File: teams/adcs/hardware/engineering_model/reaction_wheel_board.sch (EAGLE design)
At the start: 78 parts

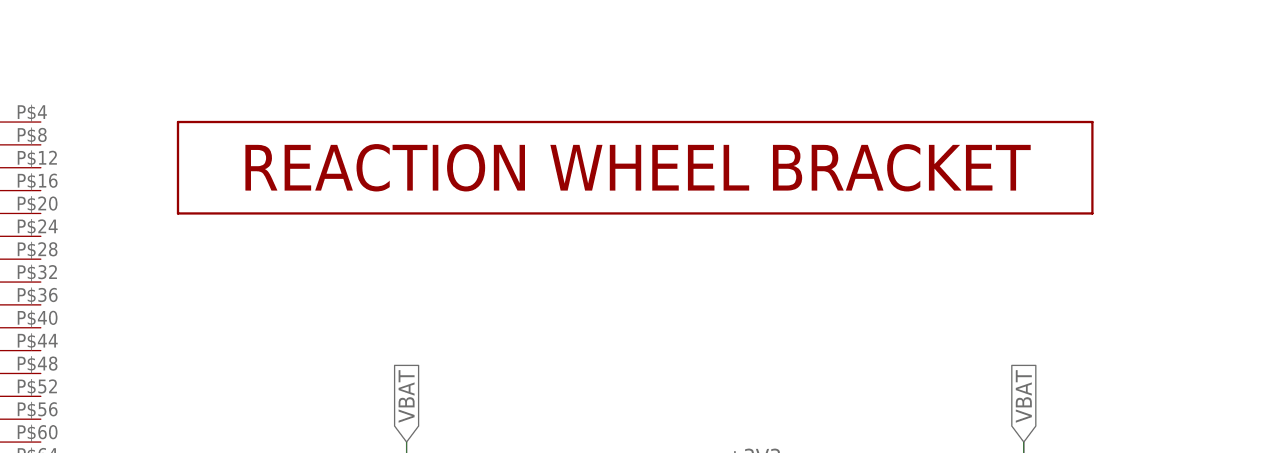
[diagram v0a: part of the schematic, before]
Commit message: ADCS/RW: Make some room for the new motor bracket
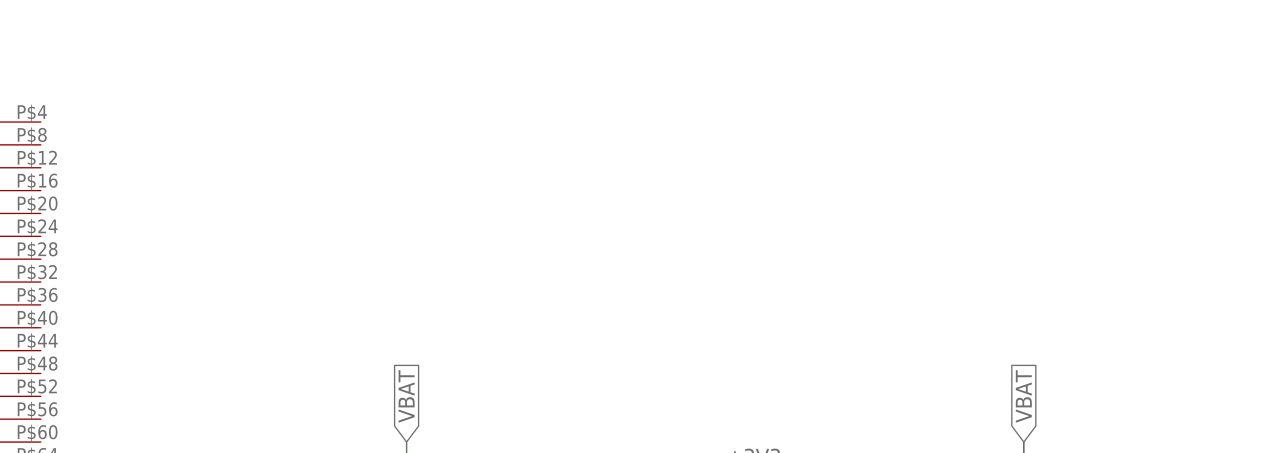
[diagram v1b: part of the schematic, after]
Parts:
- removed U$9: REACTION_WHEEL_BRACKET, DubSat1 Components:REACTION_WHEEL_BRACKET
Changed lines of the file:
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@@
 <part name="+3V1" library="supply1" library_urn="urn:adsk.eagle:library:371" deviceset="+3V3" device=""/>
 <part name="P+1" library="supply1" library_urn="urn:adsk.eagle:library:371" deviceset="+5V" device=""/>
-<part name="U$9" library="DubSat1 Components" deviceset="REACTION_WHEEL_BRACKET" device=""/>
 <part name="U$7" library="DubSat1 Components" deviceset="DRV10970" device=""/>
 <part name="C1" library="rcl" library_urn="urn:adsk.eagle:library:334" deviceset="C-US" device="C1206" package3d_urn="urn:adsk.eagle:package:23618/2" value="2.2uF"/>
@@
 <instance part="+3V1" gate="G$1" x="-63.5" y="-55.88" rot="R90"/>
 <instance part="P+1" gate="1" x="-63.5" y="-35.56" rot="R90"/>
-<instance part="U$9" gate="G$1" x="157.48" y="71.12"/>
 <instance part="U$7" gate="G$1" x="-2.54" y="-246.38" rot="R270"/>
 <instance part="C1" gate="G$1" x="15.24" y="-274.32"/>

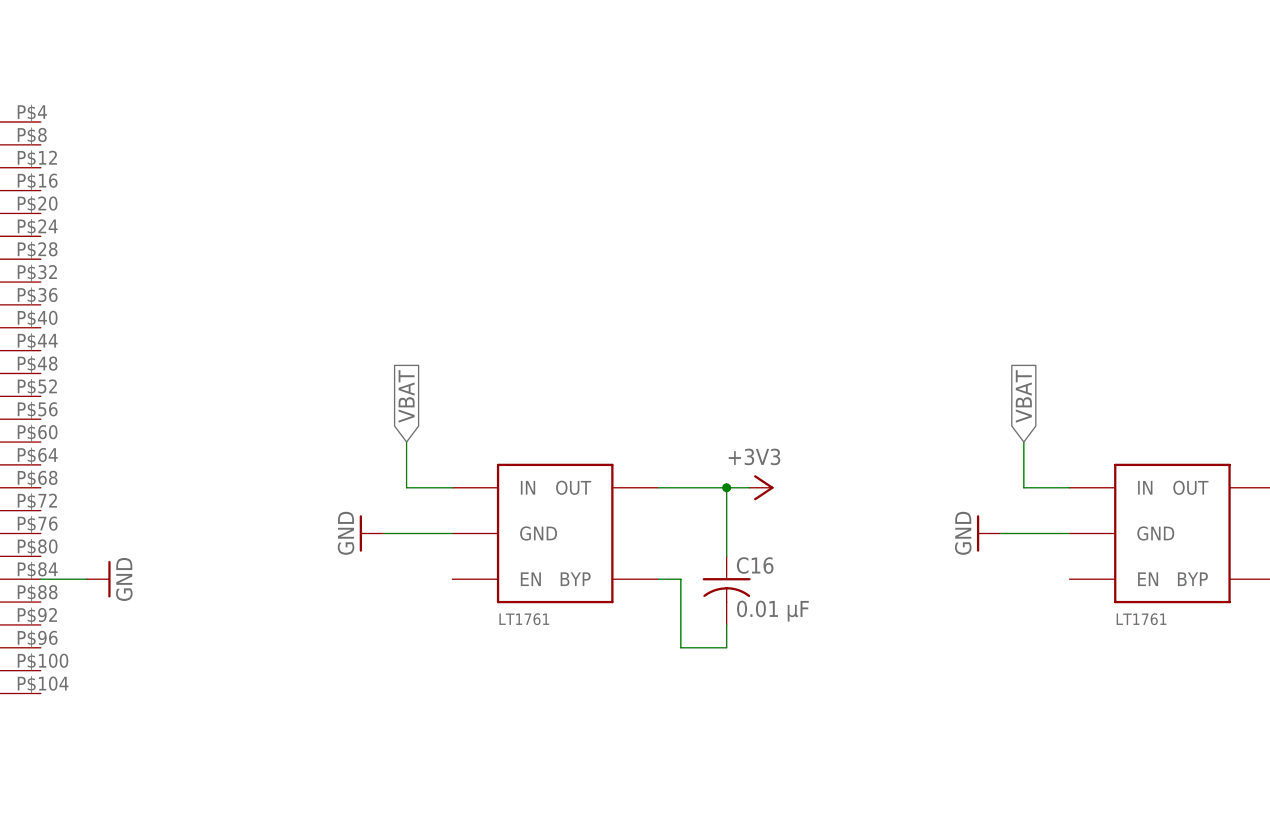
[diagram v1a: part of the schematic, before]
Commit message: ADCS/RW: Tie ENABLE pins high on LDOs
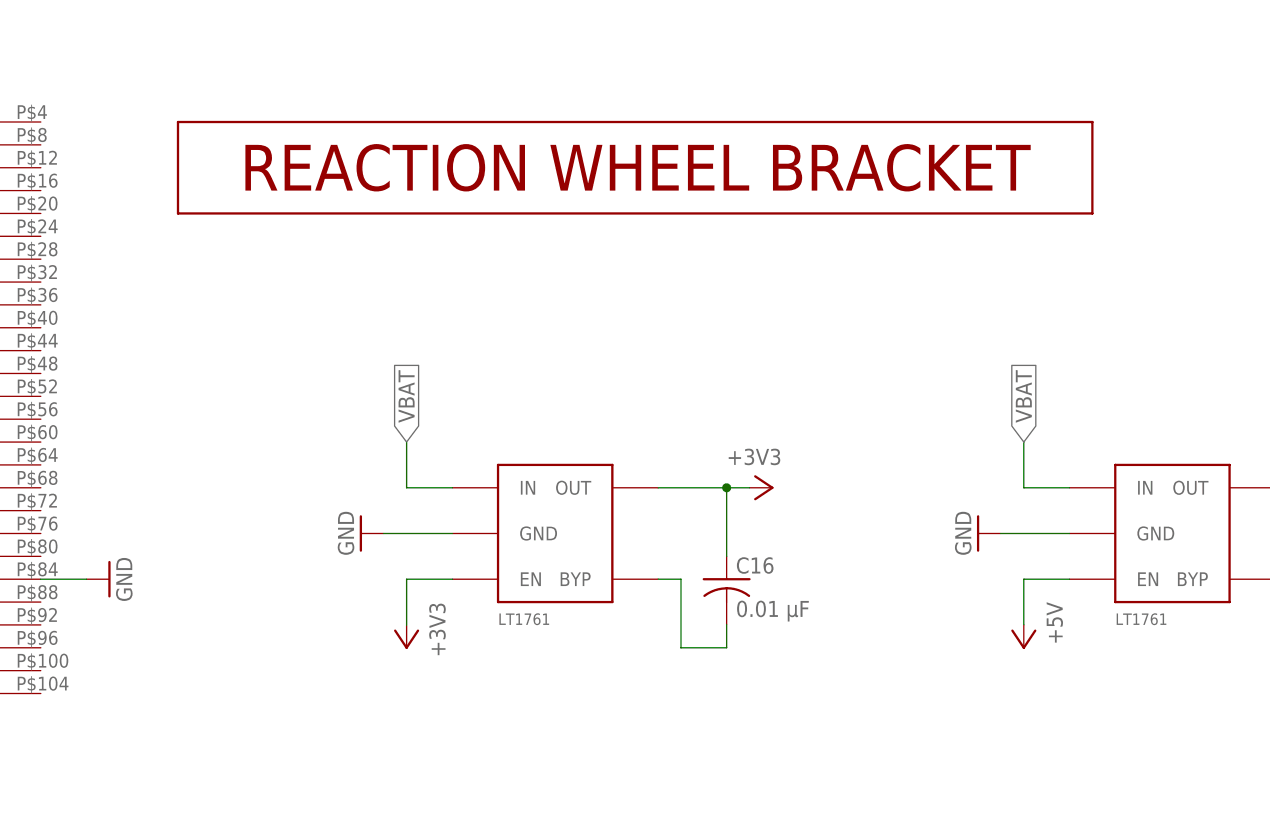
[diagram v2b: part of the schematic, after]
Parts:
- added U$9: REACTION_WHEEL_BRACKET, DubSat1 Components:REACTION_WHEEL_BRACKET
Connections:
- net +3V3: now also LDO_3V3.EN
- net +5V: now also LDO_5V.EN
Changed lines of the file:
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@@
 <part name="+3V1" library="supply1" library_urn="urn:adsk.eagle:library:371" deviceset="+3V3" device=""/>
 <part name="P+1" library="supply1" library_urn="urn:adsk.eagle:library:371" deviceset="+5V" device=""/>
+<part name="U$9" library="DubSat1 Components" deviceset="REACTION_WHEEL_BRACKET" device=""/>
 <part name="U$7" library="DubSat1 Components" deviceset="DRV10970" device=""/>
 <part name="C1" library="rcl" library_urn="urn:adsk.eagle:library:334" deviceset="C-US" device="C1206" package3d_urn="urn:adsk.eagle:package:23618/2" value="2.2uF"/>
@@
 <part name="R14" library="rcl" library_urn="urn:adsk.eagle:library:334" deviceset="R-US_" device="R0805" package3d_urn="urn:adsk.eagle:package:23553/2"/>
 <part name="GND49" library="supply1" library_urn="urn:adsk.eagle:library:371" deviceset="GND" device=""/>
+<part name="+3V2" library="supply1" library_urn="urn:adsk.eagle:library:371" deviceset="+3V3" device=""/>
+<part name="P+2" library="supply1" library_urn="urn:adsk.eagle:library:371" deviceset="+5V" device=""/>
 </parts>
 <sheets>
@@
 <instance part="+3V1" gate="G$1" x="-63.5" y="-55.88" rot="R90"/>
 <instance part="P+1" gate="1" x="-63.5" y="-35.56" rot="R90"/>
+<instance part="U$9" gate="G$1" x="157.48" y="71.12"/>
 <instance part="U$7" gate="G$1" x="-2.54" y="-246.38" rot="R270"/>
 <instance part="C1" gate="G$1" x="15.24" y="-274.32"/>
@@
 <instance part="R14" gate="G$1" x="294.64" y="45.72" rot="R90"/>
 <instance part="GND49" gate="1" x="294.64" y="38.1" rot="MR0"/>
+<instance part="+3V2" gate="G$1" x="129.54" y="17.78" rot="R180"/>
+<instance part="P+2" gate="1" x="198.12" y="17.78" rot="R180"/>
 </instances>
 <busses>
@@
 <junction x="251.46" y="-38.1"/>
 </segment>
+<segment>
+<pinref part="+3V2" gate="G$1" pin="+3V3"/>
+<pinref part="LDO_3V3" gate="G$1" pin="EN"/>
+<wire x1="129.54" y1="20.32" x2="129.54" y2="25.4" width="0.1524" layer="91"/>
+<wire x1="129.54" y1="25.4" x2="134.62" y2="25.4" width="0.1524" layer="91"/>
+</segment>
 </net>
 <net name="+5V" class="0">
@@
 <wire x1="256.54" y1="-30.48" x2="236.22" y2="-30.48" width="0.1524" layer="91"/>
 </segment>
-</net>
+<segment>
+<pinref part="P+2" gate="1" pin="+5V"/>
+<pinref part="LDO_5V" gate="G$1" pin="EN"/>
+<wire x1="198.12" y1="20.32" x2="198.12" y2="25.4" width="0.1524" layer="91"/>
+<wire x1="198.12" y1="25.4" x2="203.2" y2="25.4" width="0.1524" layer="91"/>
+</segment>
+</net>

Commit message: ADCS/RW: Tie LDO ENABLE input high
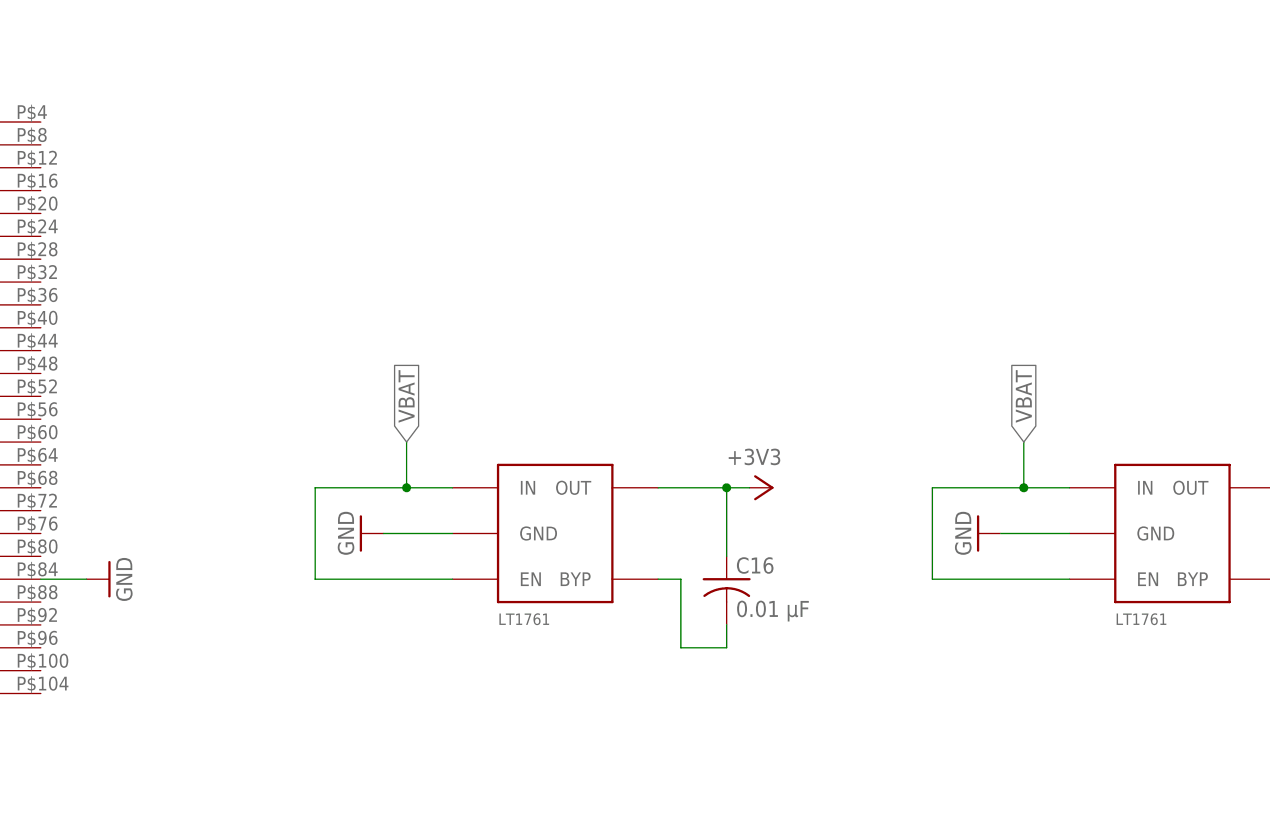
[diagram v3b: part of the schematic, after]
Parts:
- removed U$9: REACTION_WHEEL_BRACKET, DubSat1 Components:REACTION_WHEEL_BRACKET
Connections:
- net +3V3: no longer LDO_3V3.EN
- net +5V: no longer LDO_5V.EN
- net VBAT: now also LDO_3V3.EN, LDO_5V.EN
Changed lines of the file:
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@@
 <part name="+3V1" library="supply1" library_urn="urn:adsk.eagle:library:371" deviceset="+3V3" device=""/>
 <part name="P+1" library="supply1" library_urn="urn:adsk.eagle:library:371" deviceset="+5V" device=""/>
-<part name="U$9" library="DubSat1 Components" deviceset="REACTION_WHEEL_BRACKET" device=""/>
 <part name="U$7" library="DubSat1 Components" deviceset="DRV10970" device=""/>
 <part name="C1" library="rcl" library_urn="urn:adsk.eagle:library:334" deviceset="C-US" device="C1206" package3d_urn="urn:adsk.eagle:package:23618/2" value="2.2uF"/>
@@
 <part name="R14" library="rcl" library_urn="urn:adsk.eagle:library:334" deviceset="R-US_" device="R0805" package3d_urn="urn:adsk.eagle:package:23553/2"/>
 <part name="GND49" library="supply1" library_urn="urn:adsk.eagle:library:371" deviceset="GND" device=""/>
-<part name="+3V2" library="supply1" library_urn="urn:adsk.eagle:library:371" deviceset="+3V3" device=""/>
-<part name="P+2" library="supply1" library_urn="urn:adsk.eagle:library:371" deviceset="+5V" device=""/>
 </parts>
 <sheets>
@@
 <instance part="+3V1" gate="G$1" x="-63.5" y="-55.88" rot="R90"/>
 <instance part="P+1" gate="1" x="-63.5" y="-35.56" rot="R90"/>
-<instance part="U$9" gate="G$1" x="157.48" y="71.12"/>
 <instance part="U$7" gate="G$1" x="-2.54" y="-246.38" rot="R270"/>
 <instance part="C1" gate="G$1" x="15.24" y="-274.32"/>
@@
 <instance part="R14" gate="G$1" x="294.64" y="45.72" rot="R90"/>
 <instance part="GND49" gate="1" x="294.64" y="38.1" rot="MR0"/>
-<instance part="+3V2" gate="G$1" x="129.54" y="17.78" rot="R180"/>
-<instance part="P+2" gate="1" x="198.12" y="17.78" rot="R180"/>
 </instances>
 <busses>
@@
 <wire x1="129.54" y1="35.56" x2="129.54" y2="40.64" width="0.1524" layer="91"/>
 <label x="129.54" y="40.64" size="1.778" layer="95" rot="R90" xref="yes"/>
+<wire x1="129.54" y1="35.56" x2="119.38" y2="35.56" width="0.1524" layer="91"/>
+<junction x="129.54" y="35.56"/>
+<pinref part="LDO_3V3" gate="G$1" pin="EN"/>
+<wire x1="119.38" y1="35.56" x2="119.38" y2="25.4" width="0.1524" layer="91"/>
+<wire x1="119.38" y1="25.4" x2="134.62" y2="25.4" width="0.1524" layer="91"/>
 </segment>
 <segment>
@@
 <wire x1="198.12" y1="35.56" x2="198.12" y2="40.64" width="0.1524" layer="91"/>
 <label x="198.12" y="40.64" size="1.778" layer="95" rot="R90" xref="yes"/>
+<wire x1="198.12" y1="35.56" x2="187.96" y2="35.56" width="0.1524" layer="91"/>
+<junction x="198.12" y="35.56"/>
+<pinref part="LDO_5V" gate="G$1" pin="EN"/>
+<wire x1="187.96" y1="35.56" x2="187.96" y2="25.4" width="0.1524" layer="91"/>
+<wire x1="187.96" y1="25.4" x2="203.2" y2="25.4" width="0.1524" layer="91"/>
 </segment>
 <segment>
@@
 <junction x="251.46" y="-38.1"/>
 </segment>
-<segment>
-<pinref part="+3V2" gate="G$1" pin="+3V3"/>
-<pinref part="LDO_3V3" gate="G$1" pin="EN"/>
-<wire x1="129.54" y1="20.32" x2="129.54" y2="25.4" width="0.1524" layer="91"/>
-<wire x1="129.54" y1="25.4" x2="134.62" y2="25.4" width="0.1524" layer="91"/>
-</segment>
 </net>
 <net name="+5V" class="0">
@@
 <wire x1="256.54" y1="-30.48" x2="236.22" y2="-30.48" width="0.1524" layer="91"/>
 </segment>
-<segment>
-<pinref part="P+2" gate="1" pin="+5V"/>
-<pinref part="LDO_5V" gate="G$1" pin="EN"/>
-<wire x1="198.12" y1="20.32" x2="198.12" y2="25.4" width="0.1524" layer="91"/>
-<wire x1="198.12" y1="25.4" x2="203.2" y2="25.4" width="0.1524" layer="91"/>
-</segment>
-</net>
+</net>

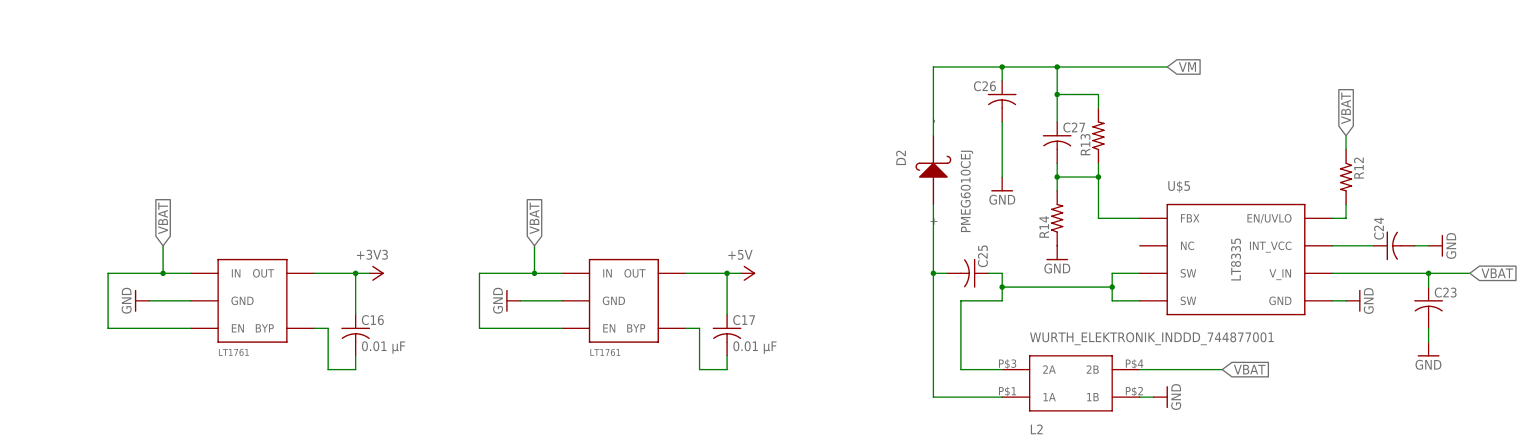
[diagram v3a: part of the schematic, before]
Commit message: ADCS/RW: Add new smoothing capacitors to LDOs
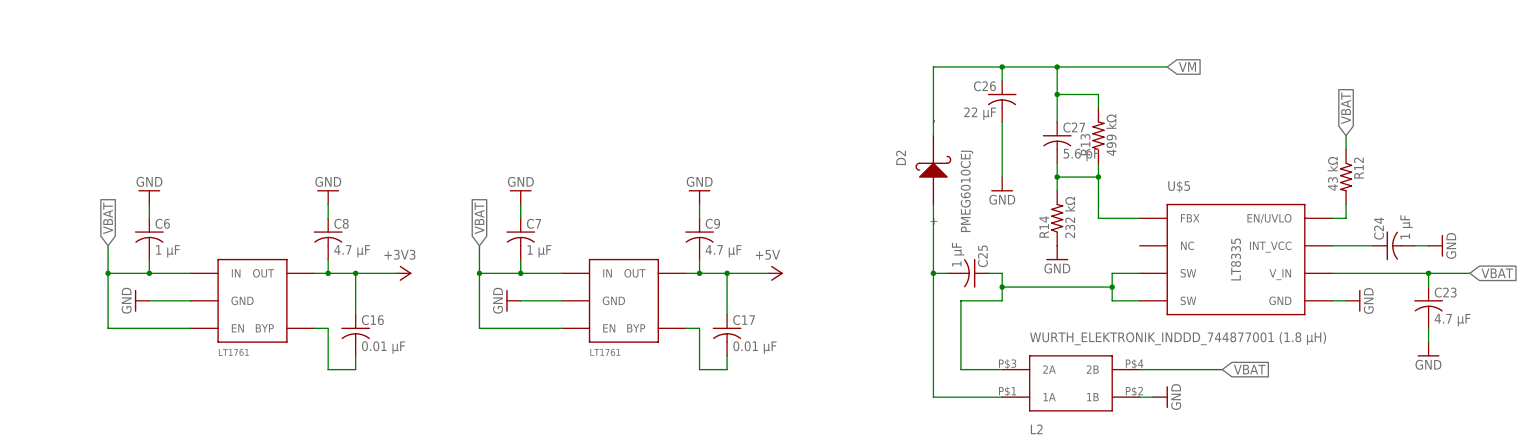
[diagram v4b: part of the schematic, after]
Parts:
- added C6, C7: 1 μF, rcl:C-USC0805
- added C8, C9: 4.7 μF, rcl:C-USC0805
- C23: value (none) -> 4.7 μF
- C24, C25: value (none) -> 1 μF
- C26: value (none) -> 22 μF
- C27: value (none) -> 5.6 pF
- L2: value WURTH_ELEKTRONIK_INDDD_744877001 -> WURTH_ELEKTRONIK_INDDD_744877001 (1.8 μH)
- R12: value (none) -> 43 kΩ
- R13: value (none) -> 499 kΩ
- R14: value (none) -> 232 kΩ
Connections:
- net +3V3: now also C8.2
- net +5V: now also C9.2
- net GND: now also C6.1, C7.1, C8.1, C9.1
- net VBAT: now also C6.2, C7.2
